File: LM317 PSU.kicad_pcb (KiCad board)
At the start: 2 copper layers, 100 x 100 mm, 58 parts, among them J1 4MM Red female, J2 4MM Black female, J3 V_IN, J4 GND, J5 Conn_01x07_Male, J6 Conn_01x07_Female, Q1 2N2222, SW1 SW_Push_SPDT, U1 NA555, U2 LM358, U3 TL061, U4 LM317_3PinPackage, U5 LM358

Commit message: Started laying out PCB
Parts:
- removed J4: GND, Connector_PinHeader_2.54mm:PinHeader_1x01_P2.54mm_Vertical
- removed J5: Conn_01x07_Male, Connector_PinHeader_2.54mm:PinHeader_1x07_P2.54mm_Vertical
- removed J6: Conn_01x07_Female, Connector_PinHeader_2.54mm:PinHeader_1x07_P2.54mm_Vertical
- added F1: Fuse, Connector_PinHeader_2.54mm:PinHeader_1x02_P2.54mm_Vertical, F.Cu at (33.0, 36.2)
- added MH7: MountingHole, MountingHole:MountingHole_3.2mm_M3, F.Cu at (236.0, 60.3)
- added MH8: MountingHole, MountingHole:MountingHole_3.2mm_M3, F.Cu at (212.6, 83.8)
- C1: value 100u 16V -> 200n; footprint Capacitor_THT:CP_Radial_D8.0mm_P3.80mm -> Capacitor_THT:C_Rect_L7.0mm_W2.5mm_P5.00mm
- C2: value 200n -> 100u 16V; footprint Capacitor_THT:C_Rect_L7.0mm_W2.5mm_P5.00mm -> Capacitor_THT:CP_Radial_D10.0mm_P3.50mm
- C3: footprint Capacitor_THT:CP_Radial_D8.0mm_P3.80mm -> Capacitor_THT:CP_Radial_D10.0mm_P3.50mm
- C5, C7: footprint Capacitor_THT:CP_Radial_D8.0mm_P5.00mm -> Capacitor_THT:CP_Radial_D5.0mm_P2.00mm
- D1, Q1: footprint Package_TO_SOT_THT:TO-92_Inline_Wide -> Package_TO_SOT_THT:TO-92L_Inline_Wide
- D2, D3: footprint Diode_THT:D_DO-35_SOD27_P7.62mm_Horizontal -> Diode_THT:D_DO-34_SOD68_P10.16mm_Horizontal
- D4: value 1N4148 -> GRN; footprint Diode_THT:D_DO-35_SOD27_P7.62mm_Horizontal -> LED_THT:LED_D5.0mm
- D5: value 1N4148 -> RED; footprint Diode_THT:D_DO-35_SOD27_P7.62mm_Horizontal -> LED_THT:LED_D5.0mm
- D6: value 5MM Green -> 1N4148; footprint LED_THT:5MM_LED -> Diode_THT:D_DO-34_SOD68_P10.16mm_Horizontal
- D7: value 5MM Red -> 1N4007; footprint LED_THT:5MM_LED -> Diode_THT:D_DO-34_SOD68_P2.54mm_Vertical_KathodeUp
- D8: value 1N4007 -> 1N4148; footprint Diode_THT:D_DO-35_SOD27_P2.54mm_Vertical_KathodeUp -> Diode_THT:D_DO-34_SOD68_P10.16mm_Horizontal
- J3: value V_IN -> Barrel_Jack_MountingPin; footprint Connector_PinHeader_2.54mm:PinHeader_1x01_P2.54mm_Vertical -> Connector_BarrelJack:BarrelJack_Horizontal
- MH1, MH2, MH3, MH4, MH5, MH6: footprint MountingHole:MountingHole_3.2mm_M3_ISO7380 -> MountingHole:MountingHole_3.2mm_M3
- R1, R10, R11, R13, R16, R3, R7, R8, R9: footprint Resistor_THT:R_Axial_DIN0207_L6.3mm_D2.5mm_P7.62mm_Horizontal -> Resistor_THT:R_Axial_DIN0207_L6.3mm_D2.5mm_P10.16mm_Horizontal
- R12: value 3.3K -> 1K; footprint Resistor_THT:R_Axial_DIN0207_L6.3mm_D2.5mm_P7.62mm_Horizontal -> Resistor_THT:R_Axial_DIN0207_L6.3mm_D2.5mm_P10.16mm_Horizontal
- R14: value 10R -> 10K; footprint Resistor_THT:R_Axial_DIN0207_L6.3mm_D2.5mm_P7.62mm_Horizontal -> Resistor_THT:R_Axial_DIN0207_L6.3mm_D2.5mm_P10.16mm_Horizontal
- R15: value 1K -> 3K3; footprint Resistor_THT:R_Axial_DIN0207_L6.3mm_D2.5mm_P7.62mm_Horizontal -> Resistor_THT:R_Axial_DIN0207_L6.3mm_D2.5mm_P10.16mm_Horizontal
- R17: value 10K -> 10R; footprint Resistor_THT:R_Axial_DIN0207_L6.3mm_D2.5mm_P7.62mm_Horizontal -> Resistor_THT:R_Axial_DIN0207_L6.3mm_D2.5mm_P10.16mm_Horizontal
- R2, R4, R6: value 2.2K -> 2K2; footprint Resistor_THT:R_Axial_DIN0207_L6.3mm_D2.5mm_P7.62mm_Horizontal -> Resistor_THT:R_Axial_DIN0207_L6.3mm_D2.5mm_P10.16mm_Horizontal
- R5: value 0R22 1W MIN -> 0R22 1W
- RV1, RV2: footprint Connector_PinHeader_2.54mm:PinHeader_1x03_P2.54mm_Vertical -> Potentiometer_THT:Potentiometer_Alps_RK09K_Single_Vertical
- U2: value LM358 -> TL061
- U3: value TL061 -> LM358
- moved D5 127.8 mm to (226.5, 71.8)
- moved D4 125.7 mm to (234.5, 68.0)
- moved C5 125.2 mm to (29.0, 54.0)
- moved D7 123.5 mm to (33.0, 60.5), turned to 270 degrees
- moved D6 114.6 mm to (48.3, 57.8), turned to 180 degrees
- moved C6 114.1 mm to (33.0, 65.6), turned to 270 degrees
- moved D1 100.8 mm to (233.9, 46.0)
- moved SW1 96.5 mm to (218.4, 56.6)
- moved U2 94.9 mm to (38.1, 33.7)
- moved R16 94.4 mm to (48.3, 76.2), turned to 180 degrees
- moved C7 94.0 mm to (29.1, 73.0)
- moved RV3 87.3 mm to (54.6, 66.7), turned to 180 degrees
- moved MH1 86.2 mm to (236.4, 52.3)
- moved Q1 85.4 mm to (66.0, 83.2), turned to 180 degrees
- moved U4 84.5 mm to (27.9, 65.6), turned to 90 degrees
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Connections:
- C1 pad 1: Net-(C1-Pad1) -> GNDA
- C2 pad 2: GNDA -> Net-(C2-Pad2)
- C7 pad 1: /OUTPUT -> OUTPUT
- D2 pad 1: Net-(C1-Pad1) -> Net-(C2-Pad1)
- D3 pad 2: Net-(C1-Pad1) -> Net-(C2-Pad1)
- D4 pad 1: /I_set -> LED
- D4 pad 2: /V_ADJ -> Net-(D4-Pad2)
- D5 pad 1: /V_set -> Net-(D5-Pad1)
- D5 pad 2: /V_ADJ -> LED
- D6 pad 1: LED -> /I_cmp
- D6 pad 2: Net-(D6-Pad2) -> /V_ADJ
- D7 pad 1: Net-(D7-Pad1) -> /REG_INP
- D7 pad 2: LED -> OUTPUT
- D8 pad 1: /REG_INP -> /V_cmp
- D8 pad 2: /OUTPUT -> /V_ADJ
- J1 pad 1: /OUTPUT -> OUTPUT
- MES2 pad 2: /OUTPUT -> OUTPUT
- Q1 pad 3: /OUTPUT -> OUTPUT
- R1 pad 1: +12V -> 2V5
- R1 pad 2: 2V5 -> +12V
- R10 pad 1: 2V5 -> Net-(R10-Pad1)
- R10 pad 2: Net-(R10-Pad2) -> 2V5
- R11 pad 1: Net-(R11-Pad1) -> Net-(R10-Pad1)
- R11 pad 2: Net-(R10-Pad2) -> Net-(R11-Pad2)
- R12 pad 1: /OUTPUT -> GNDA
- R12 pad 2: Net-(R12-Pad2) -> Net-(D5-Pad1)
- R13 pad 1: Net-(R12-Pad2) -> +12V
- R13 pad 2: GNDA -> Net-(D4-Pad2)
- R14 pad 1: /I_sink_sense -> GNDA
- R14 pad 2: V- -> Net-(D4-Pad2)
- R15 pad 1: Net-(D7-Pad1) -> Net-(R15-Pad1)
- R15 pad 2: GNDA -> OUTPUT
- R16 pad 1: +12V -> GNDA
- R16 pad 2: Net-(D6-Pad2) -> Net-(R15-Pad1)
- R17 pad 1: Net-(D6-Pad2) -> V-
- R17 pad 2: GNDA -> /I_sink_sense
- R2 pad 1: +12V -> Net-(F1-Pad1)
- R4 pad 2: Net-(C2-Pad1) -> Net-(C1-Pad2)
- R5 pad 1: +12V -> /REG_INP
- R5 pad 2: /REG_INP -> Net-(F1-Pad1)
- R8 pad 1: /I_SENSE -> /Lo_side_sense
- R8 pad 2: /Lo_side_sense -> I_FB
- R9 pad 1: 2V5 -> Net-(R10-Pad1)
- R9 pad 2: Net-(R10-Pad2) -> 2V5
- RV1 pad 3: Net-(R11-Pad1) -> Net-(R11-Pad2)
- SW1 pad 1: /I_SENSE -> I_FB
- U1 pad 2: Net-(C2-Pad1) -> Net-(C1-Pad2)
- U1 pad 3: Net-(C1-Pad2) -> Net-(C2-Pad2)
- U1 pad 5: Net-(U1-Pad5) -> (no net)
- U1 pad 6: Net-(C2-Pad1) -> Net-(C1-Pad2)
- U2 pad 1: Net-(Q1-Pad2) -> (no net)
- U2 pad 2: /I_sink_sense -> /Lo_side_sense
- U2 pad 3: Net-(RV3-Pad2) -> /Hi_side_sense
- U2 pad 5: I_SET -> (no net)
- U2 pad 6: /I_SENSE -> I_FB
- U2 pad 7: /I_set -> +12V
- U2 pad 8: +12V -> (no net)
- U3 pad 1: Net-(U3-Pad1) -> /V_cmp
- U3 pad 2: /Lo_side_sense -> Net-(R15-Pad1)
- U3 pad 3: /Hi_side_sense -> V_SET
- U3 pad 5: Net-(U3-Pad5) -> I_SET
- U3 pad 6: /I_SENSE -> I_FB
- U3 pad 7: +12V -> /I_cmp
- U3 pad 8: Net-(U3-Pad8) -> +12V
- U4 pad 2: /OUTPUT -> OUTPUT
- U5 pad 1: /V_set -> Net-(Q1-Pad2)
- U5 pad 2: Net-(R12-Pad2) -> /I_sink_sense
- U5 pad 3: V_SET -> Net-(RV3-Pad2)
- U5 pad 4: GNDA -> V-
- U5 pad 5: /V_set -> /V_cmp
- U5 pad 6: /I_set -> /I_cmp
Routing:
- net OUTPUT: track 0.00 -> 67.2 mm
- net /I_cmp: track 0.00 -> 39.9 mm, vias 0 -> 1
- net I_FB: track 0.00 -> 38.9 mm
- net /V_cmp: track 0.00 -> 38.3 mm, vias 0 -> 1
- net /REG_INP: track 0.00 -> 35.0 mm
- net /Lo_side_sense: track 0.00 -> 34.7 mm
- net +12V: track 0.00 -> 28.1 mm
- net Net-(R15-Pad1): track 0.00 -> 22.6 mm
- net Net-(Q1-Pad2): track 0.00 -> 21.9 mm
- net /Hi_side_sense: track 0.00 -> 18.1 mm
- net /V_ADJ: track 0.00 -> 16.7 mm
- net Net-(F1-Pad1): track 0.00 -> 13.9 mm
- net Net-(RV3-Pad2): track 0.00 -> 8.83 mm
- net /I_sink_sense: track 0.00 -> 3.81 mm
- added copper zone on F.Cu, net +12V
- added copper zone on F.Cu, net /REG_INP
- added copper zone on B.Cu, net GNDA
- added copper zone on F.Cu, net OUTPUT
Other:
- net class Default: clearance 0.2 -> 0.5; trace_width 0.25 -> 0.5; via_dia 1 -> 1.2
- net class PWR: clearance 0.2 -> 0.5; trace_width 1 -> 2; via_dia 1.6 -> 2; via_drill 1 -> 0.8
- rule trace_clearance: 0.2 -> 0.5

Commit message: main board almost complete
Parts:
- moved MH5 169.9 mm to (45.0, 25.0)
- moved MH3 159.7 mm to (45.0, 95.0)
- moved C8 154.7 mm to (50.8, 64.1), turned to 180 degrees
- moved MH2 151.0 mm to (75.0, 25.0)
- moved D4 143.4 mm to (91.4, 57.1), turned to 180 degrees
- moved D5 143.0 mm to (88.9, 33.0)
- moved MH4 141.5 mm to (90.0, 95.0)
- moved MH8 138.0 mm to (75.0, 95.0)
- moved MH6 137.0 mm to (90.0, 25.0)
- moved C9 132.6 mm to (66.0, 58.4), turned to 270 degrees
- moved R12 104.8 mm to (83.2, 22.9), turned to 270 degrees
- moved D1 103.5 mm to (131.6, 61.5), turned to 180 degrees
- moved MH1 97.5 mm to (145.6, 16.7)
- moved MH7 97.5 mm to (145.2, 24.7)
- moved RV1 83.1 mm to (87.5, 38.1), turned to 270 degrees
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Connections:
- RV1 pad 1: GNDA -> Net-(R11-Pad2)
- RV1 pad 3: Net-(R11-Pad2) -> GNDA
- RV2 pad 1: GNDA -> 2V5
- RV2 pad 3: 2V5 -> GNDA
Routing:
- net V-: track 0.00 -> 92.3 mm
- net +12V: track 28.1 -> 84.8 mm, vias 0 -> 2
- net Net-(C1-Pad2): track 0.00 -> 30.0 mm, vias 0 -> 1
- net Net-(C2-Pad1): track 0.00 -> 24.4 mm, vias 0 -> 1
- net /I_sink_sense: track 3.81 -> 20.4 mm, vias 0 -> 1
- net Net-(C2-Pad2): track 0.00 -> 16.6 mm
- net Net-(R3-Pad2): track 0.00 -> 14.5 mm
- net /I_cmp: track 39.9 -> 47.4 mm
- net I_FB: track 38.9 -> 45.2 mm
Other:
- board size 100 x 100 mm -> 100 x 80 mm

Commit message: Rev 1 mostly complete
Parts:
- removed MH6, MH7: MountingHole, MountingHole:MountingHole_3.2mm_M3
- added J4: Conn_01x07_Male, Connector_PinHeader_2.54mm:PinHeader_1x07_P2.54mm_Vertical, F.Cu at (128.6, 82.9)
- added J5: Conn_01x07_Female, Connector_PinHeader_2.54mm:PinHeader_1x07_P2.54mm_Vertical, F.Cu at (151.4, 82.9)
- added J6: Conn_01x01_Female, TestPoint:TestPoint_Loop_D3.50mm_Drill1.4mm_Beaded, F.Cu at (148.9, 72.7)
- added J7: Conn_01x01_Female, TestPoint:TestPoint_Loop_D3.50mm_Drill1.4mm_Beaded, F.Cu at (148.3, 37.8)
- moved U3 137.2 mm to (172.4, 92.4), turned to 90 degrees
- moved U2 136.5 mm to (172.4, 58.1), turned to 90 degrees
- moved C3 136.4 mm to (191.4, 38.4), turned to 270 degrees
- moved F1 133.2 mm to (166.1, 30.2), turned to 270 degrees
- moved R5 132.4 mm to (160.3, 42.9), turned to 90 degrees
- moved D2 130.0 mm to (183.8, 50.5), turned to 0 degrees
- moved C2 129.0 mm to (191.4, 31.1), turned to 90 degrees
- moved C5 127.4 mm to (155.9, 42.3), turned to 90 degrees
- moved R2 126.8 mm to (164.8, 50.5), turned to 270 degrees
- moved D3 126.7 mm to (177.5, 46.7), turned to 0 degrees
- moved MH5 126.0 mm to (171.0, 25.0)
- moved R17 125.5 mm to (180.0, 97.5), turned to 180 degrees
- moved U1 125.4 mm to (183.8, 35.2), turned to 180 degrees
- moved C8 125.4 mm to (174.9, 81.6)
- moved C4 124.5 mm to (168.6, 50.5), turned to 90 degrees
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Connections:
- C4 pad 2: +12V -> 12V_F
- C8 pad 2: +12V -> 12V_F
- C9 pad 2: +12V -> 12V_F
- F1 pad 1: Net-(F1-Pad1) -> 12V_F
- R1 pad 2: +12V -> 12V_F
- R13 pad 1: +12V -> 12V_F
- R2 pad 1: Net-(F1-Pad1) -> 12V_F
- R3 pad 1: +12V -> 12V_F
- R5 pad 2: Net-(F1-Pad1) -> 12V_F
- U1 pad 4: +12V -> 12V_F
- U1 pad 5: (no net) -> Net-(U1-Pad5)
- U1 pad 8: +12V -> 12V_F
- U2 pad 1: (no net) -> Net-(U2-Pad1)
- U2 pad 5: (no net) -> Net-(U2-Pad5)
- U2 pad 7: +12V -> 12V_F
- U2 pad 8: (no net) -> Net-(U2-Pad8)
- U3 pad 1: /V_cmp -> LED
- U3 pad 2: Net-(R15-Pad1) -> /I_cmp
- U3 pad 3: V_SET -> /V_cmp
- U3 pad 5: I_SET -> Net-(RV3-Pad2)
- U3 pad 6: I_FB -> /I_sink_sense
- U3 pad 7: /I_cmp -> Net-(Q1-Pad2)
- U3 pad 8: +12V -> 12V_F
- U5 pad 1: Net-(Q1-Pad2) -> /I_cmp
- U5 pad 2: /I_sink_sense -> I_FB
- U5 pad 3: Net-(RV3-Pad2) -> I_SET
- U5 pad 5: /V_cmp -> V_SET
- U5 pad 6: /I_cmp -> Net-(R15-Pad1)
- U5 pad 7: LED -> /V_cmp
- U5 pad 8: +12V -> 12V_F
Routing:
- net 12V_F: track 0.00 -> 258.6 mm, vias 0 -> 5
- net I_SET: track 0.00 -> 170.0 mm, vias 0 -> 4
- net 2V5: track 0.00 -> 168.8 mm, vias 0 -> 2
- net LED: track 0.00 -> 164.7 mm, vias 0 -> 3
- net I_FB: track 45.2 -> 206.8 mm, vias 0 -> 4
- net V_SET: track 0.00 -> 107.9 mm, vias 0 -> 2
- net V-: track 92.3 -> 0.00 mm
- net +12V: track 84.8 -> 8.25 mm, vias 2 -> 0
- net /V_cmp: track 38.3 -> 69.1 mm
- net Net-(R11-Pad2): track 0.00 -> 26.3 mm
- net Net-(D4-Pad2): track 0.00 -> 25.2 mm, vias 0 -> 1
- net GNDA: track 0.00 -> 24.6 mm, vias 0 -> 2
- net Net-(D5-Pad1): track 0.00 -> 23.1 mm
- net OUTPUT: track 67.2 -> 86.2 mm, vias 0 -> 3
- net /I_sink_sense: track 20.4 -> 38.5 mm, vias 1 -> 0
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- added copper zone on F.Cu, net 12V_F
- added copper zone on F.Cu, net GNDA
- added copper zone on F.Cu, net V-
- removed copper zone on F.Cu, net +12V
- removed copper zone on F.Cu, net /REG_INP
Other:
- board size 100 x 80 mm -> 177.5 x 90 mm
- board text added: "CC"
- board text added: "CV"
- board text added: "POWER CONNECTORS"

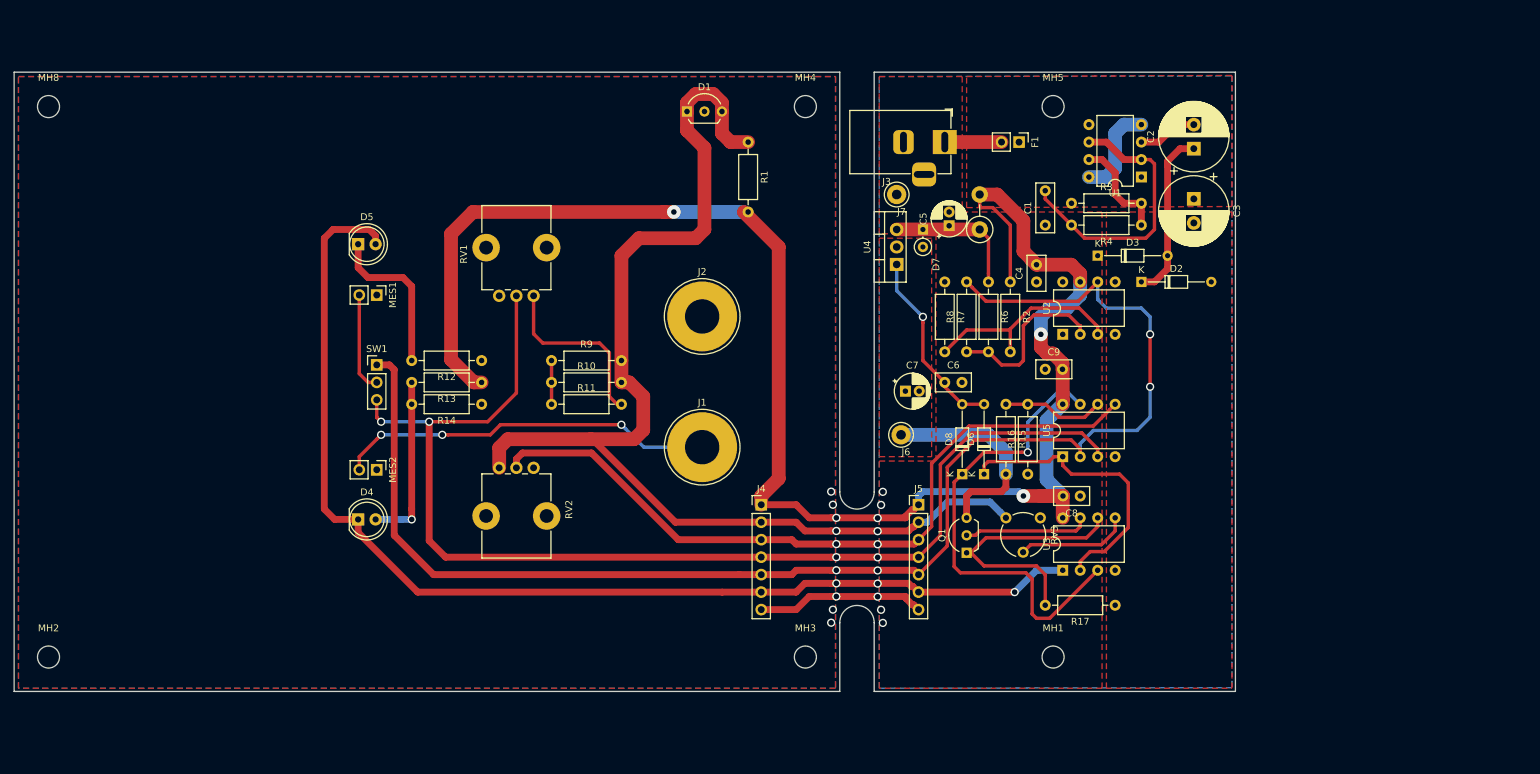
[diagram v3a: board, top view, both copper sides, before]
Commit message: added cut outs for meters, started arranging silkscreen
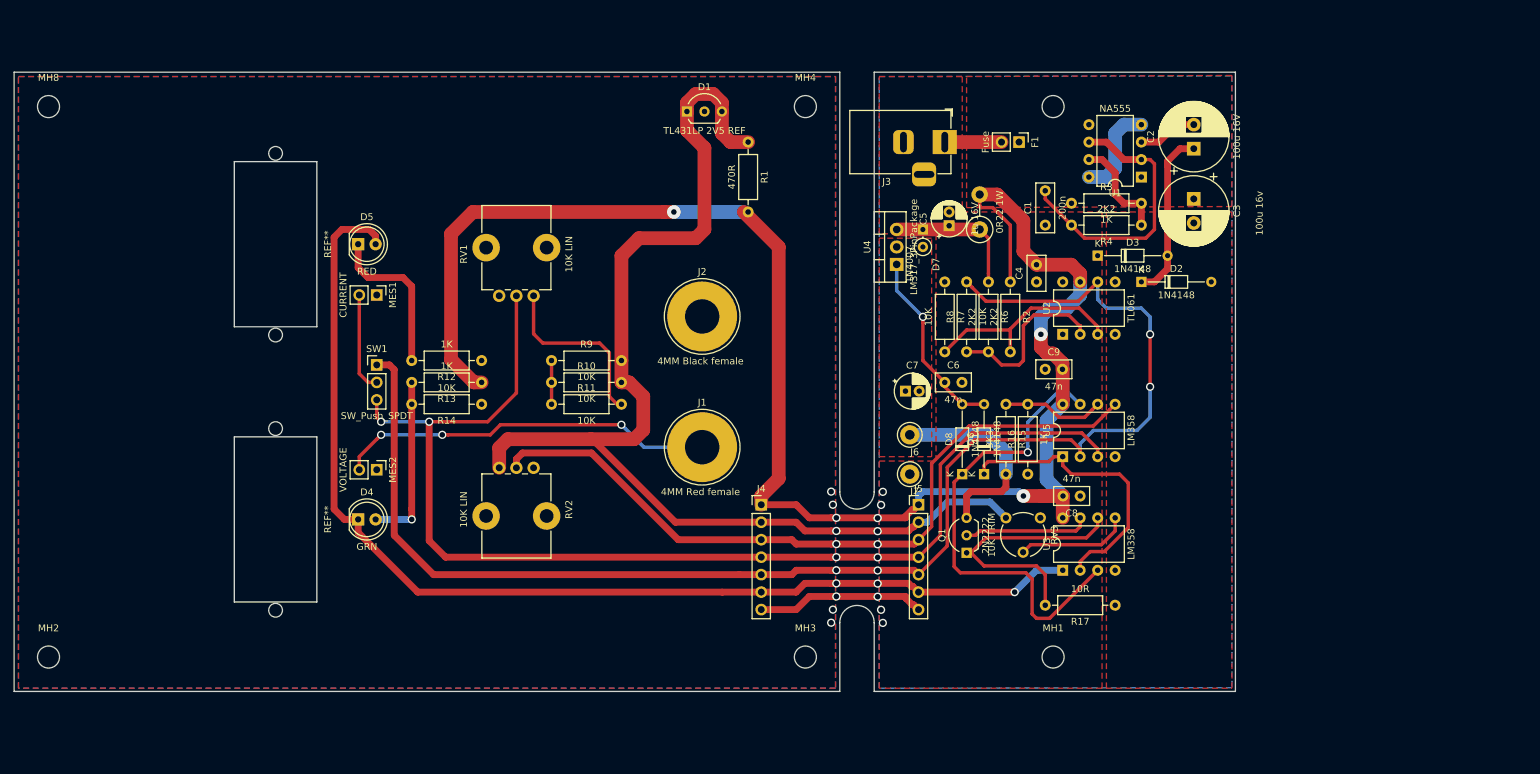
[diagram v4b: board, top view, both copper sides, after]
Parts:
- added REF**: 3 DIGIT PANEL METER, PS2:3 DIGIT PANEL METER, F.Cu at (58.0, 45.0)
- added REF**: 3 DIGIT PANEL METER, PS2:3 DIGIT PANEL METER, F.Cu at (58.0, 85.0)
- moved J7 40.7 mm to (150.2, 78.4)
- moved J6 1.27 mm to (150.2, 72.7)
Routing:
- net LED: track 164.7 -> 162.0 mm
- net OUTPUT: track 86.2 -> 84.5 mm
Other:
- outline, holes or cut-outs redrawn

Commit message: REV B SENT FOR PROTOTYPING, ADDED NEG RAIL REGULATOR
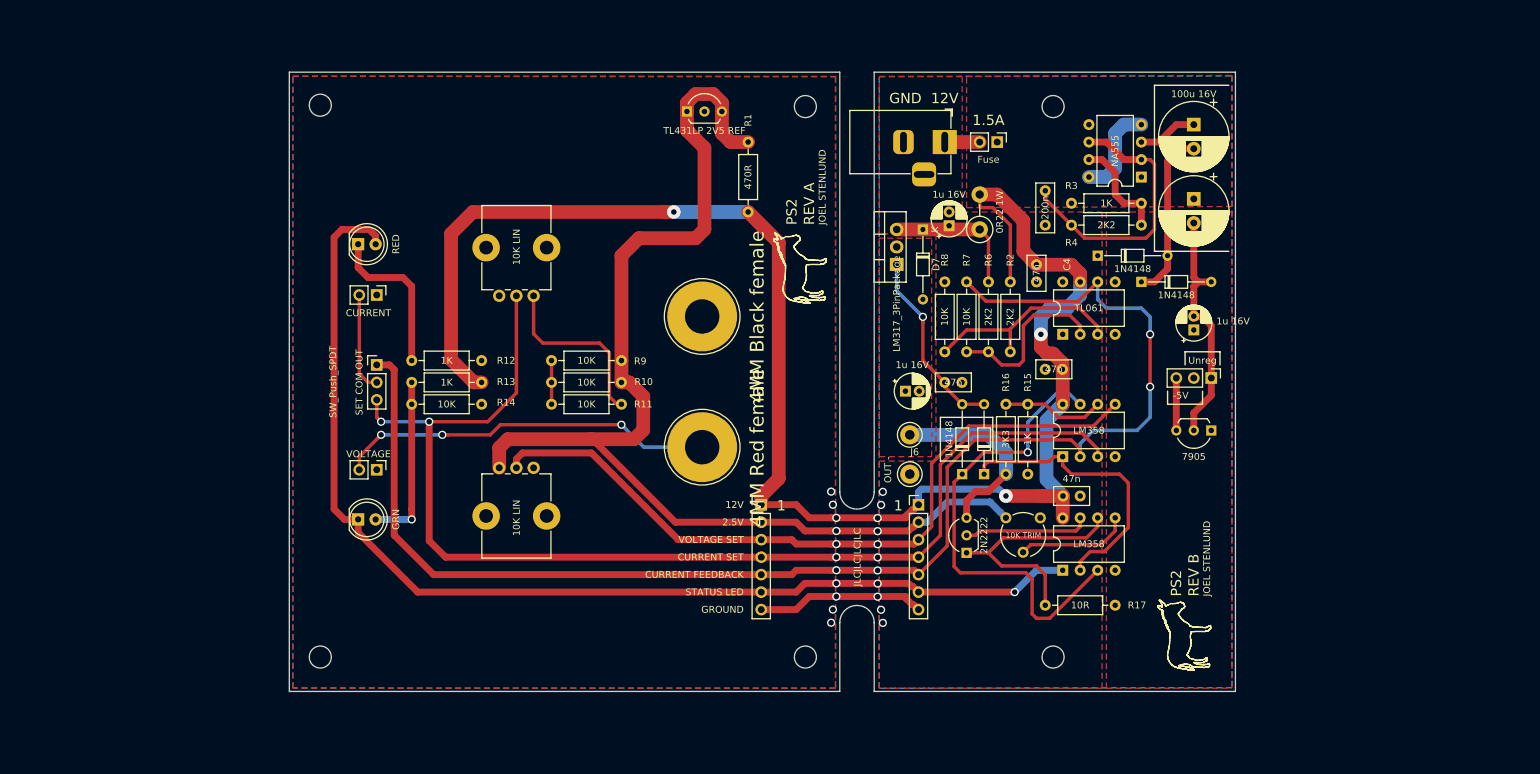
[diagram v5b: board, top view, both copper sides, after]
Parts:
- removed REF** (x2): 3 DIGIT PANEL METER, PS2:3 DIGIT PANEL METER
- added C10: 1u 16V, Capacitor_THT:CP_Radial_D5.0mm_P2.00mm, F.Cu at (191.4, 57.5)
- added J8: V- jumper, Connector_PinHeader_2.54mm:PinHeader_1x03_P2.54mm_Vertical, F.Cu at (194.0, 64.5)
- added U6: 7905, Package_TO_SOT_THT:TO-92L_Inline_Wide, F.Cu at (194.0, 72.1)
- D7: footprint Diode_THT:D_DO-34_SOD68_P2.54mm_Vertical_KathodeUp -> Diode_THT:D_DO-34_SOD68_P10.16mm_Horizontal
- moved MH8 39.5 mm to (64.5, 24.8)
- moved MH2 39.5 mm to (64.5, 105.0)
- moved C2 3.50 mm to (191.4, 27.6), turned to 270 degrees
- moved F1 3.18 mm to (162.9, 30.2)
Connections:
- C3 pad 2: V- -> Net-(C10-Pad2)
- D2 pad 1: Net-(C2-Pad1) -> Net-(C2-Pad2)
- D2 pad 2: V- -> Net-(C10-Pad2)
- D3 pad 2: Net-(C2-Pad1) -> Net-(C2-Pad2)
- U1 pad 3: Net-(C2-Pad2) -> Net-(C2-Pad1)
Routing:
- net Net-(C10-Pad2): track 0.00 -> 35.1 mm
- net Net-(C2-Pad2): track 8.67 -> 24.8 mm
- net Net-(C2-Pad1): track 24.8 -> 8.67 mm
- net Net-(J8-Pad3): track 0.00 -> 7.62 mm
- net +12V: track 8.25 -> 5.08 mm
- net /I_sink_sense: track 38.5 -> 35.9 mm
- net OUTPUT: track 84.5 -> 83.0 mm
- net 12V_F: track 258.6 -> 259.6 mm
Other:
- board size 177.5 x 90 mm -> 137.5 x 90 mm
- rule via_min_size: 0.4 -> 0.45
- board text added: "-5V"
- board text added: "1"
- board text added: "1.5A"
- board text added: "12V"
- board text added: "2.5V"
- board text added: "CURRENT FEEDBACK"
- board text added: "CURRENT SET"
- board text added: "GND"
- board text added: "GROUND"
- board text added: "JLCJLCJLCJLC"
- board text added: "JOEL STENLUND"
- board text added: "PS2"
- board text added: "REV A"
- board text added: "REV B"
- board text added: "SET COM OUT"
- board text added: "STATUS LED"
- board text added: "Unreg"
- board text added: "VOLTAGE SET"
- board text removed: "CC"
- board text removed: "CV"
- board text removed: "POWER CONNECTORS"
